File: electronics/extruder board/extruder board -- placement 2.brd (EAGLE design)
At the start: 35 x 51.2 mm, 22 parts, among them IC1 MAX6675, IC2 MAX6675, J1 Main THERMO, J2 AUX THERMO, J3 Main Heater, J4 Secondary HEATER, X1 22-23-2041, X2 Right Fan, X3 Left Fan, X4 Extruder Fan

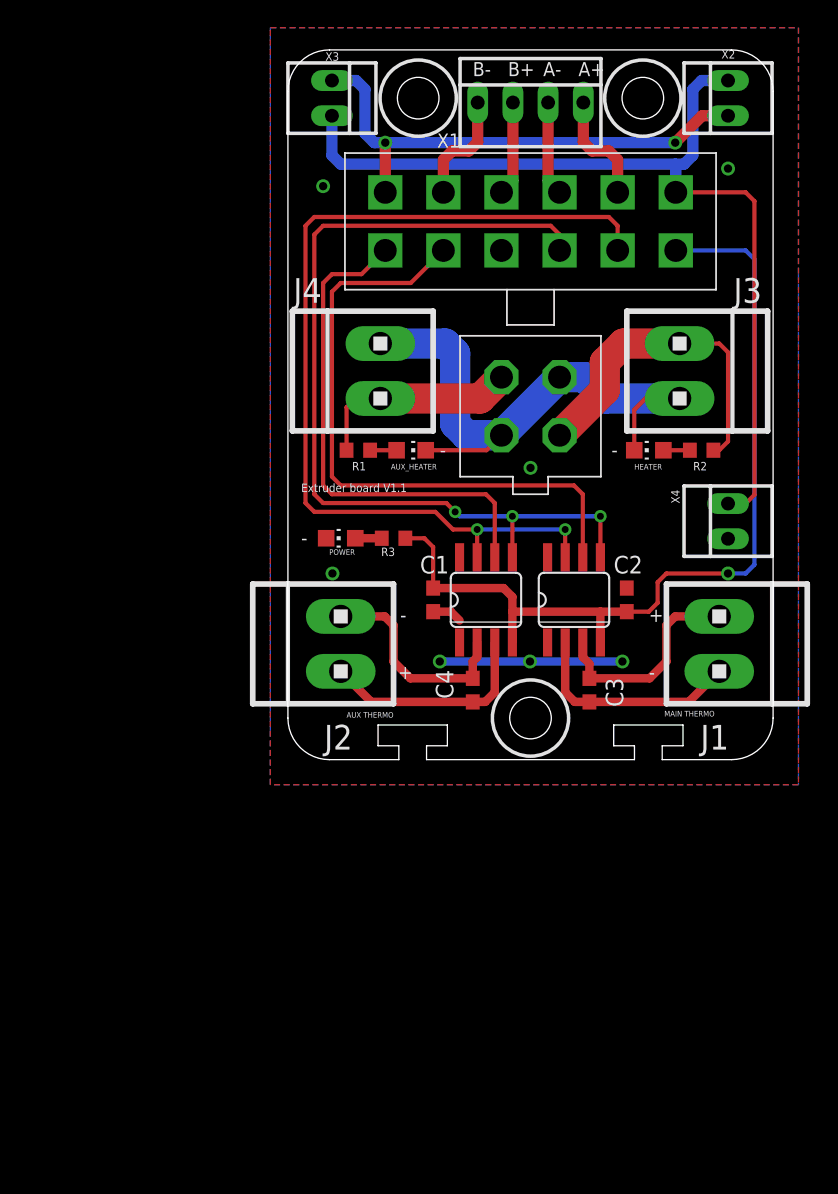
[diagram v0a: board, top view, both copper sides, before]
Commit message: Extruder board V1.2
-Changed harness pin assignment
-Added nozzle fan driver and using pin CS1 as control signal
-Added invert circuit and using pin CS2 to control both thermocouple ADC
-Isolated the AUX heater GND and Heater GND
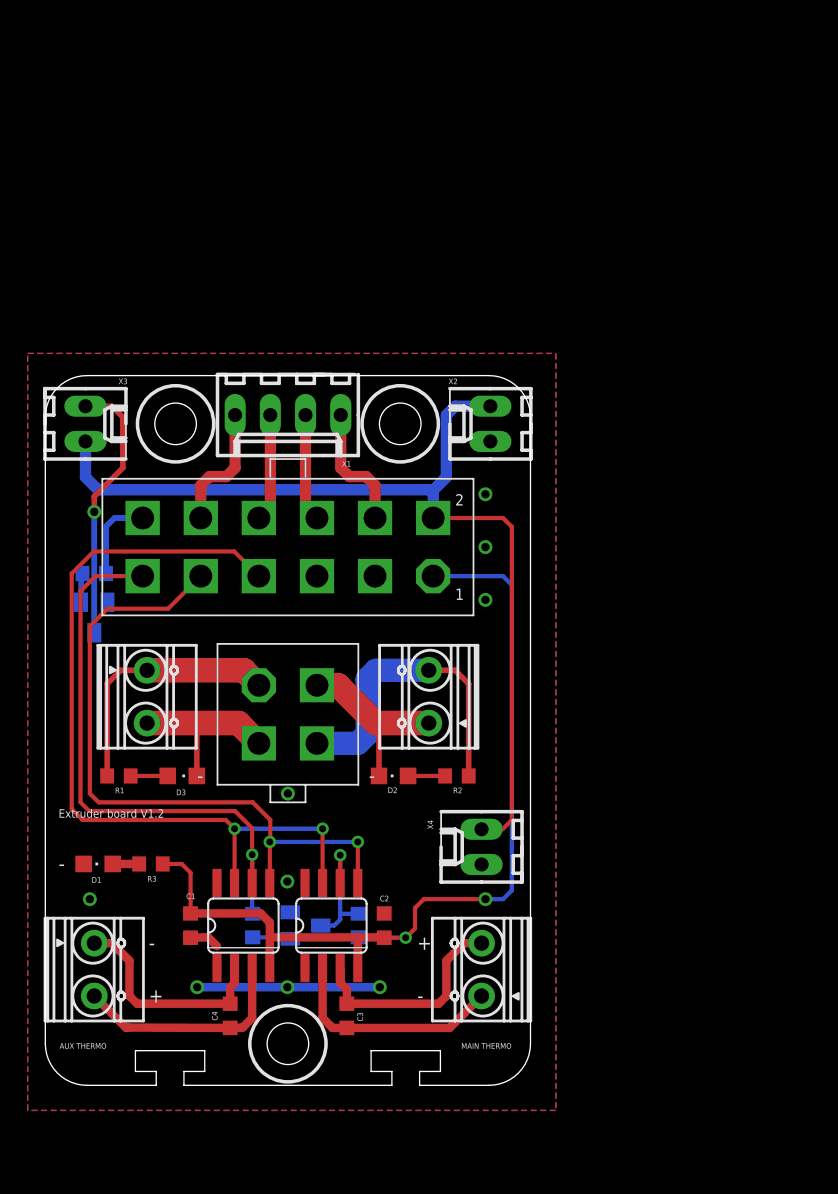
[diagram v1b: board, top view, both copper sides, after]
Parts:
- removed AUX_HEATER: AUX HEATER, led:CHIP-LED0805
- removed HEATER: HEATER, led:CHIP-LED0805
- removed J1: Main THERMO, 555 delay toggle switch:CON-AMP_1X2MTA
- removed J2: AUX THERMO, 555 delay toggle switch:CON-AMP_1X2MTA
- removed J3: Main Heater, 555 delay toggle switch:CON-AMP_1X2MTA
- removed J4: Secondary HEATER, 555 delay toggle switch:CON-AMP_1X2MTA
- removed POWER: POWER, led:CHIP-LED0805
- removed U$1: MOLEX_5557_6X2, extruder lib:MOLEX_5557
- removed U$3: MOLEX_5557_2X2, extruder board -- placement 2:MOLEX_5557_2X2
- added D1: POWER, extruder_board_--_placement_2:CHIPLED_0805
- added D2: HEATER, extruder_board_--_placement_2:CHIPLED_0805
- added D3: AUX HEATER, extruder_board_--_placement_2:CHIPLED_0805
- added Q1, Q2: BC817-16SMD, extruder_board_--_placement_2:SOT23-BEC
- added R4, R5, R6: 1K, extruder_board_--_placement_2:R0603
- added X10: 5557-12, extruder_board_--_placement_2:5557-12
- added X5, X6, X7, X8: 1727010, extruder_board_--_placement_2:1727010
- added X9: 5557-04, extruder_board_--_placement_2:5557-04
- C1, C2, C3, C4: device rcl:C0603 -> extruder_board_--_placement_2:C0603K
- IC1, IC2: device adafruit:SO08 -> extruder_board_--_placement_2:SO-8
- R1, R2, R3: device rcl:R0603 -> extruder_board_--_placement_2:R0603
- X1: value 22-23-2041 -> 22-27-2041-04; device con-molex:22-23-2041 -> extruder_board_--_placement_2:6410-04
- X2: value Right Fan -> LED_12V; device con-molex:22-23-2021 -> extruder_board_--_placement_2:6410-02
- X3: value Left Fan -> Nozzel Fan; device con-molex:22-23-2021 -> extruder_board_--_placement_2:6410-02
- X4: device con-molex:22-23-2021 -> extruder_board_--_placement_2:6410-02
- moved X3 29.5 mm to (-14.6, 22.2)
- moved X4 29.5 mm to (14.0, -8.29)
- moved R2 29.4 mm to (12.2, -3.17)
- moved C1 29.3 mm to (-7.02, -14.0)
- moved C2 29.3 mm to (6.95, -14.0)
- moved C3 29.3 mm to (4.25, -20.5)
- moved C4 29.3 mm to (-4.17, -20.5)
- moved IC1 29.3 mm to (3.14, -14.0)
- moved IC2 29.3 mm to (-3.21, -14.0)
- moved R3 29.3 mm to (-9.88, -9.53)
- moved R1 29.2 mm to (-12.2, -3.17)
- moved X2 29.1 mm to (14.6, 22.2)
- moved X1 28.5 mm to (0.00, 22.9), turned to 180 degrees
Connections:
- removed net COOLING_FANS: U$1.12, X2.1, X3.1
- removed net CS1!: IC1.6, U$1.9
- removed net CS2!: IC2.6, U$1.11
- removed net DO: IC1.7, IC2.7, U$1.3
- removed net VCC: C1.1, C2.1, IC1.4, IC2.4, R3.1, U$1.1
- new net !CS2: IC1.6, Q1.C, R5.1
- new net +5V: C1.1, C2.1, IC1.4, IC2.4, R3.1, R5.2, X10.1
- new net -FAN: Q2.C, X3.2
- new net AUX_HEATER_GND: D3.C, X5.2, X9.2
- new net CS1: R6.1, X10.12
- new net CS2: IC2.6, R4.1, X10.11
- new net MISO: IC1.7, IC2.7, X10.7
- new net MOSI: X10.5
- new net N$6: Q1.B, R4.2
- new net N$9: Q2.B, R6.2
- net +12V: now also X10.2, X2.1, X3.1, X4.1; no longer U$1.2, X2.2, X3.2, X4.2
- net AUX_HEATER: now also X5.1, X9.1; no longer J4.2, U$3.4
- net GND: now also D1.C, Q1.E, Q2.E, X10.3, X2.2, X4.2; no longer POWER.C, U$1.7, X4.1
- net HEATER: now also X6.2, X9.4; no longer J3.2, U$3.1
- net HEATER_GND: now also D2.C, X6.1, X9.3; no longer AUX_HEATER.C, HEATER.C, J3.1, J4.1, U$3.2, U$3.3
- net MOTOR_A+: now also X10.4; no longer U$1.4
- net MOTOR_A-: now also X10.6; no longer U$1.6
- net MOTOR_B+: now also X10.8; no longer U$1.8
- net MOTOR_B-: now also X10.10; no longer U$1.10
- net N$1: now also X8.1; no longer J2.1
- net N$2: now also X7.1; no longer J1.1
- net N$3: now also X7.2; no longer J1.2
- net N$4: now also X8.2; no longer J2.2
- net N$5: now also D1.A; no longer POWER.A
- net N$7: now also D2.A; no longer HEATER.A
- net N$8: now also D3.A; no longer AUX_HEATER.A
- net SCK: now also X10.9; no longer U$1.5
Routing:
- net DO: track 68.4 -> 0.00 mm, vias 2 -> 0
- net +5V: track 0.00 -> 67.9 mm, vias 0 -> 2
- net VCC: track 64.4 -> 0.00 mm, vias 1 -> 0
- net MISO: track 0.00 -> 58.4 mm, vias 0 -> 2
- net CS1!: track 45.8 -> 0.00 mm
- net CS2: track 0.00 -> 41.6 mm, vias 0 -> 1
- net CS2!: track 36.9 -> 0.00 mm
- net COOLING_FANS: track 36.7 -> 0.00 mm, vias 2 -> 0
- net HEATER_GND: track 42.1 -> 13.1 mm
- net -FAN: track 0.00 -> 19.4 mm, vias 0 -> 1
- net SCK: track 65.3 -> 49.3 mm, vias 3 -> 2
- net AUX_HEATER_GND: track 0.00 -> 12.5 mm
- net !CS2: track 0.00 -> 9.54 mm, vias 0 -> 1
- net CS1: track 0.00 -> 6.29 mm
- net AUX_HEATER: track 15.2 -> 18.4 mm
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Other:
- board text added: "+5V"
- board text added: "Extruder board V1.2"
- board text added: "MISO"
- board text added: "MOSI"
- board text removed: "DO"
- board text removed: "Extruder board V1.1"
- board text removed: "FAN"
- board text removed: "VCC"

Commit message: Extruder board V1.3
1. remove the T style cutouts in the front
2. Added holes for filament insert
3. extended board size
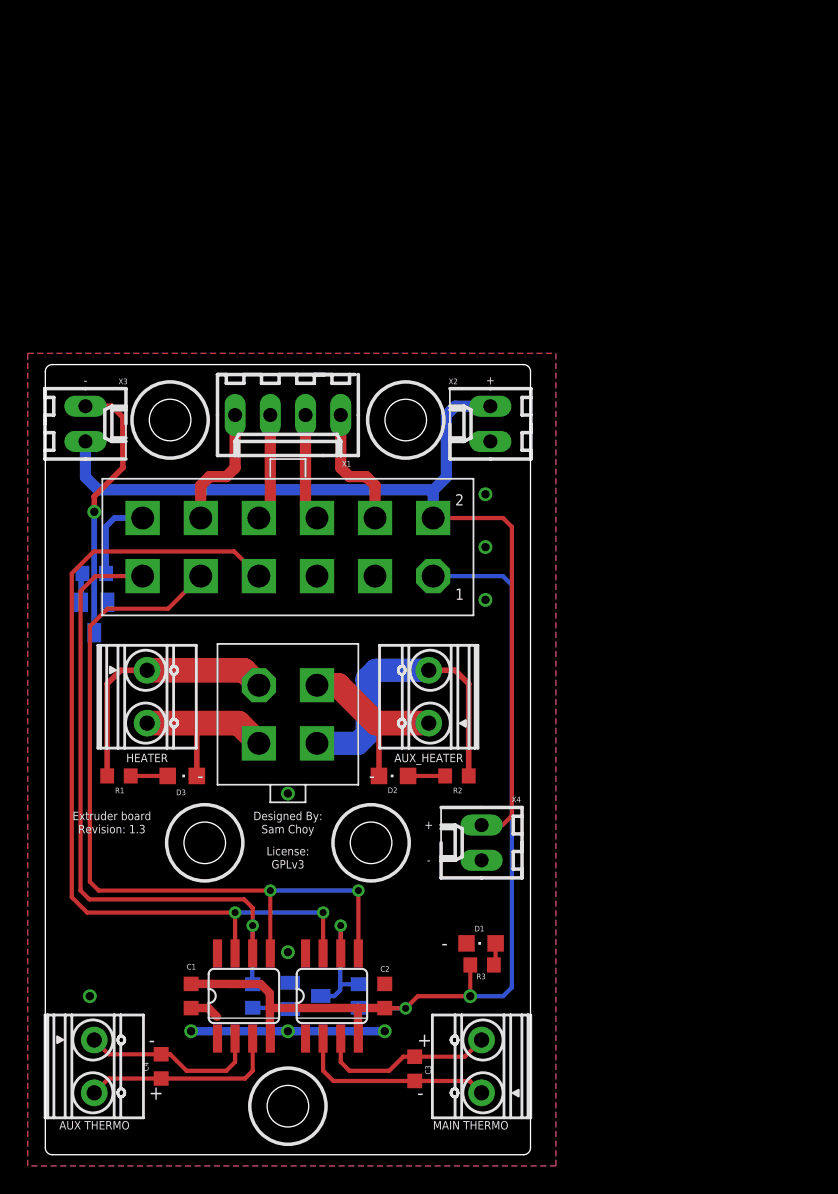
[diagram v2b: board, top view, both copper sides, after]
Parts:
- moved D1 28.2 mm to (13.9, -15.3)
- moved R3 25.0 mm to (14.0, -16.8), turned to 0 degrees
- moved X7 6.98 mm to (14.0, -24.1)
- moved X8 6.98 mm to (-14.0, -24.1)
- moved C3 6.21 mm to (9.14, -24.3)
- moved C4 6.17 mm to (-9.14, -24.1)
- moved C1 5.08 mm to (-6.99, -19.1)
- moved C2 5.08 mm to (6.99, -19.1)
- moved IC1 5.08 mm to (3.17, -19.1)
- moved IC2 5.08 mm to (-3.17, -19.1)
- moved Q1 5.08 mm to (1.27, -19.1)
- moved R4 5.08 mm to (-2.54, -19.1)
- moved R5 5.08 mm to (5.08, -19.1)
- moved X4 0.30 mm to (14.0, -7.99)
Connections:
- net AUX_HEATER: now also R2.1, X6.2, X9.4; no longer R1.1, X5.1, X9.1
- net AUX_HEATER_GND: now also D2.C, X6.1, X9.3; no longer D3.C, X5.2, X9.2
- net HEATER: now also R1.1, X5.1, X9.1; no longer R2.1, X6.2, X9.4
- net HEATER_GND: now also D3.C, X5.2, X9.2; no longer D2.C, X6.1, X9.3
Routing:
- net SCK: track 49.3 -> 56.6 mm
- net CS2: track 41.6 -> 47.0 mm
- net MISO: track 58.4 -> 62.7 mm
- net HEATER: track 22.5 -> 18.4 mm
- net AUX_HEATER: track 18.4 -> 22.5 mm
- net N$1: track 15.8 -> 13.0 mm
- net N$3: track 15.8 -> 13.0 mm
- net +5V: track 67.9 -> 70.2 mm
- net N$2: track 16.3 -> 14.4 mm
- net N$4: track 16.2 -> 14.4 mm
- net GND: track 15.3 -> 16.1 mm
- net HEATER_GND: track 13.1 -> 12.5 mm
- net AUX_HEATER_GND: track 12.5 -> 13.1 mm
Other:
- board size 35 x 51.2 mm -> 35 x 57 mm
- board text added: "AUX_HEATER"
- board text added: "Designed By:"
- board text added: "Extruder board"
- board text added: "GPLv3"
- board text added: "HEATER"
- board text added: "License:"
- board text added: "Revision: 1.3"
- board text added: "Sam Choy"
- board text removed: "Extruder board V1.2"
